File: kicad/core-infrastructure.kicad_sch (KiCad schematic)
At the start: 8 parts, among them J2 T-Connector Deans 14 AWG, SW2 Latching Push Button, U5 PCA9685PW, U6 JZK 2S 7.4V 8A BMS, U7 MP1584 Buck Converter 5V, U8 ESP32-S3 Super Mini

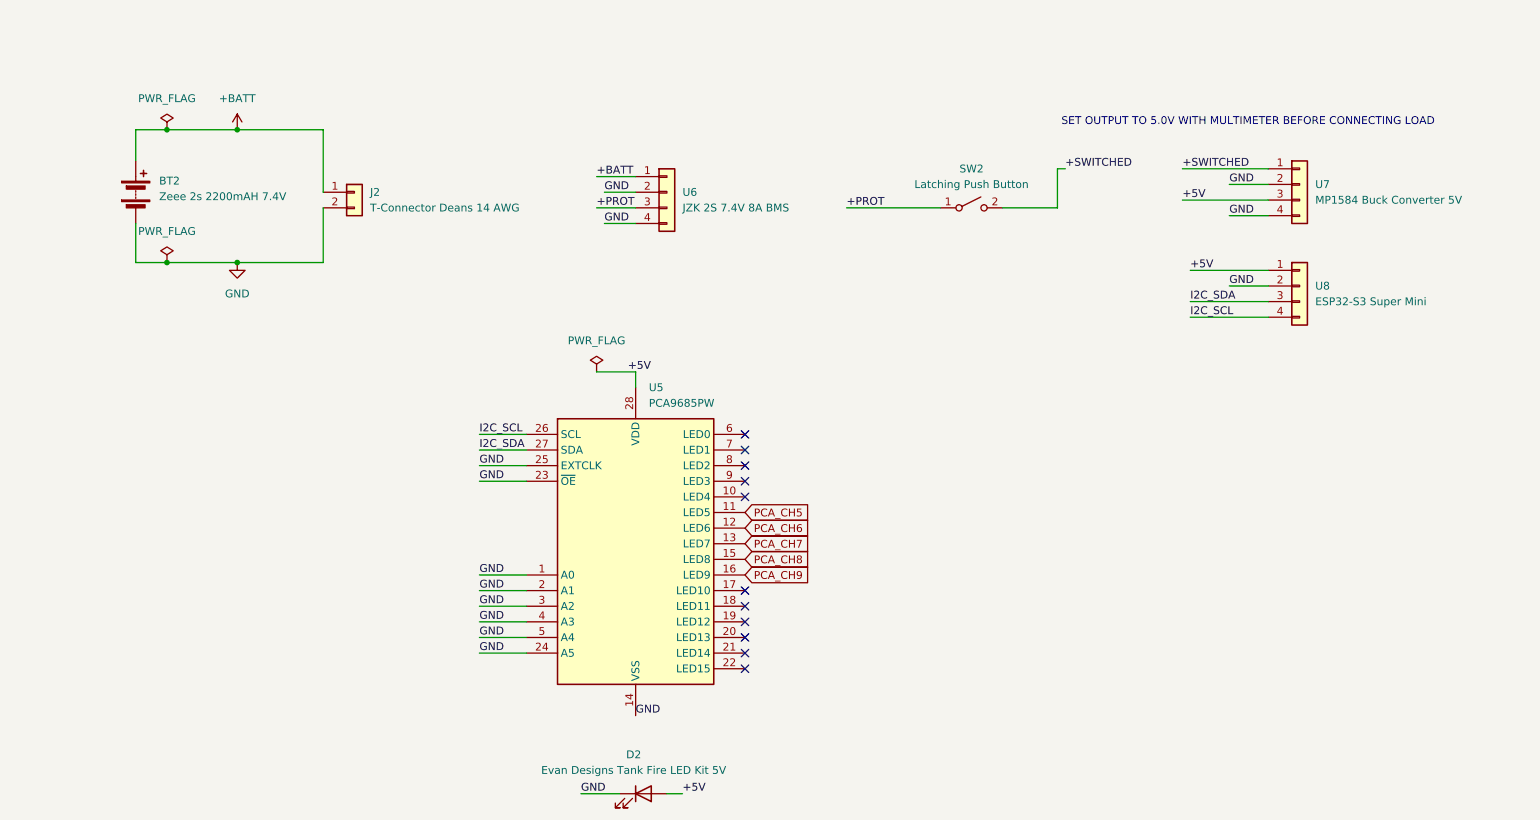
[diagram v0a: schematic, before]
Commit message: docs: simplify power chain — remove BMS, add low-voltage alarm
- Remove BMS from power chain; battery internal protection is sufficient
  for this low-current display application
- Add LiPo low-voltage alarm on JST-XH balance lead for overdischarge warning
- Update wire gauge table to reflect battery → switch → buck chain
- Note that switch pre-soldered leads (~26 AWG) must be replaced with
  14 AWG stranded wire
- Simplify build guide Steps 1-2 to match new power chain
- Update core-infrastructure schematic and re-export SVG

Co-Authored-By: Claude Sonnet 4.6 <noreply@anthropic.com>
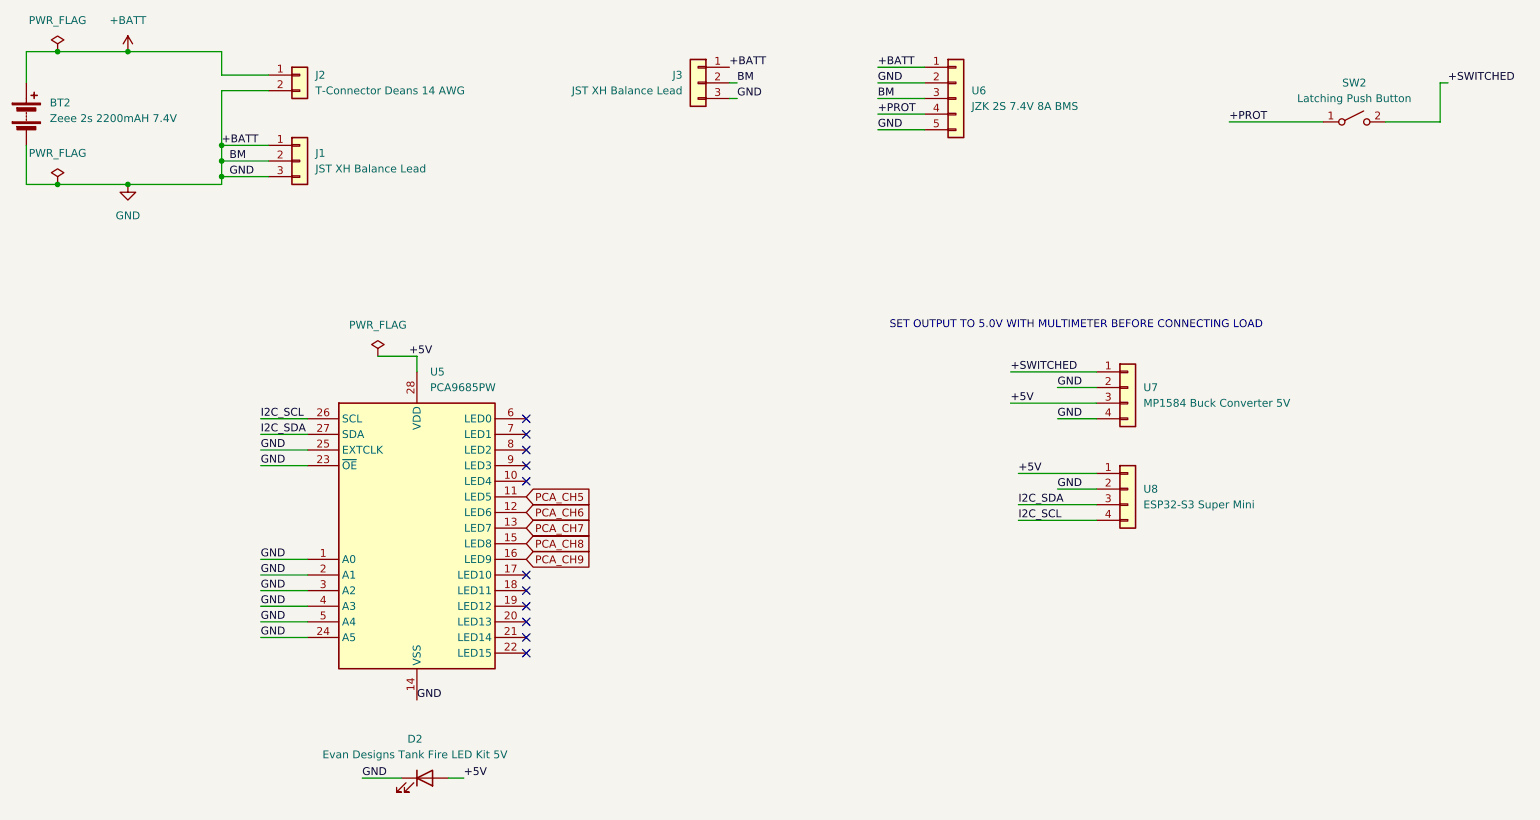
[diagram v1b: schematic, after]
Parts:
- removed U6: JZK 2S 7.4V 8A BMS, symbol Connector_Generic:Conn_01x04
- added J1, J3: JST XH Balance Lead, symbol Connector_Generic:Conn_01x03
- added U6: JZK 2S 7.4V 8A BMS, symbol Connector_Generic:Conn_01x05
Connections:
- net GND is gone; now on net +BATT: BT2.2 (-), D2.1 (K), J2.2 (Pin_2), U5.1 (A0), U5.14 (VSS), U5.2 (A1), U5.23 (~{OE}), U5.24 (A5), U5.25 (EXTCLK), U5.3 (A2), U5.4 (A3), U5.5 (A4), U7.2 (Pin_2), U7.4 (Pin_4), U8.2 (Pin_2)
- net +BATT: now also J1.1 (Pin_1), J1.2 (Pin_2), J1.3 (Pin_3), J3.1 (Pin_1), J3.2 (Pin_2), J3.3 (Pin_3), U6.1 (Pin_1), U6.2 (Pin_2), U6.3 (Pin_3), U6.5 (Pin_5)
- net +PROT: now also U6.4 (Pin_4)
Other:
- moved on the sheet: BT2, D2, J2, SW2, U5, U7, U8
